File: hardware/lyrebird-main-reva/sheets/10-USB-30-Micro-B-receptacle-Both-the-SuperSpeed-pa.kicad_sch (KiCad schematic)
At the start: 4 parts, among them J1 Connfly DS1104-01

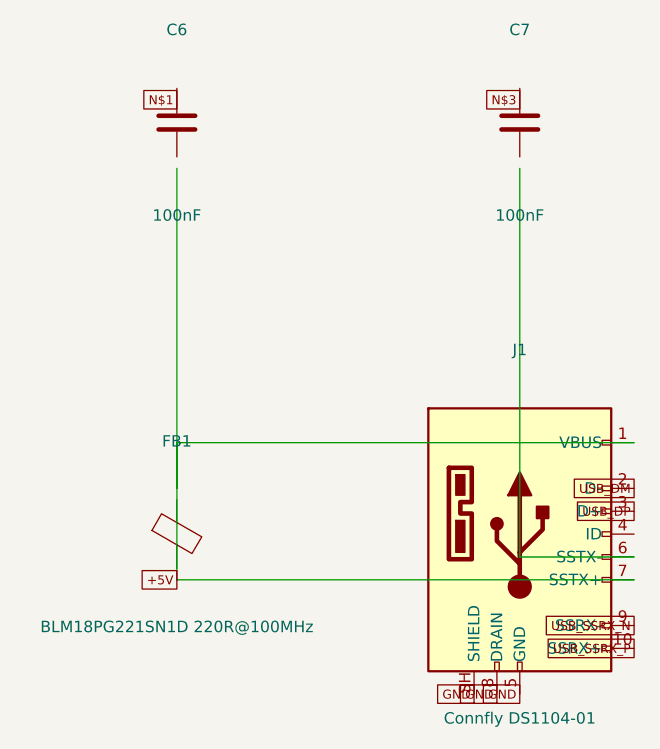
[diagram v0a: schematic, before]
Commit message: Regenerate the schematics, which were eleven days behind the netlists
The sheets and both PDFs dated 13 September against netlists from
today. They showed a board with USB bus power, a charge pump on the
analog module, no JTAG series protection, no oscillator pull-downs and
none of the footprint corrections -- a board that has not existed for
some time. Anyone opening them to review the design would have been
reviewing the wrong one, which is worse than having no schematic.

Regenerated from the current netlists: the main board goes from 8
sheets to 11, picking up the wall-wart input and the inverter, and the
module from 6 to 9 while losing the charge pump entirely. Both PDFs
rebuilt through kicad-cli, one page per sheet.

Nothing regenerated them because nothing was watching. The netlist
generators are run constantly and the views derived from them are not,
so they drift silently and there is no check that notices.

Co-Authored-By: Claude Opus 5 <noreply@anthropic.com>
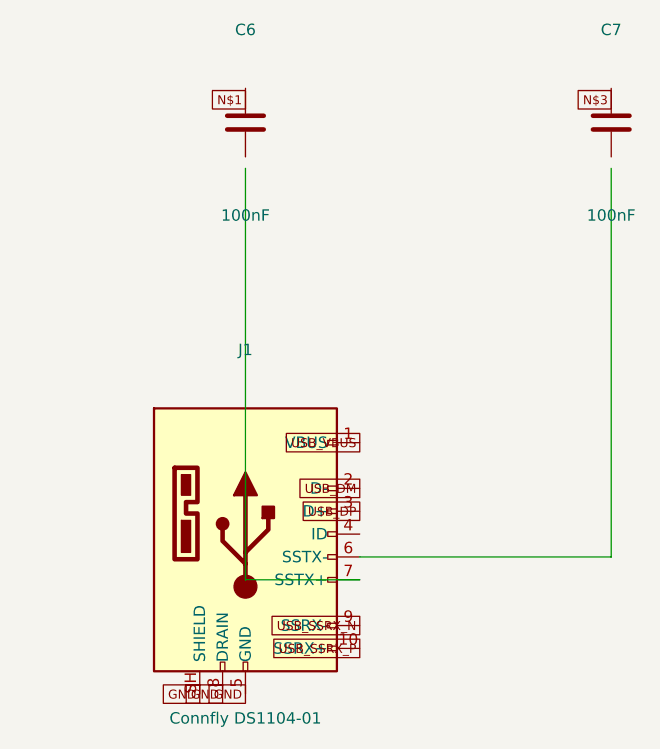
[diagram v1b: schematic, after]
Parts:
- removed J1: Connfly DS1104-01, symbol Connector:USB3_B_Micro
- J1: renamed from FB1; value BLM18PG221SN1D 220R@100MHz -> Connfly DS1104-01; symbol Device:FerriteBead -> Connector:USB3_B_Micro
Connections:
- net GND: now also J1.5 (GND), J1.8 (DRAIN), J1.SH (SHIELD)
- net USB_DM: now also J1.2 (D-)
- net USB_DP: now also J1.3 (D+)
- net USB_SSRX_N: now also J1.9 (SSRX-)
- net USB_SSRX_P: now also J1.10 (SSRX+)
- net USB_VBUS: now reaches J1.1 (VBUS)
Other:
- moved on the sheet: C6, C7
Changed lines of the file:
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@@
 	(paper "User" 132 128)
 	(title_block (title "USB 3.0 Micro-B receptacle. Both the SuperSpeed pairs and the"))
-	(symbol (lib_id "Device:C") (at 35.56 35.56 0) (unit 1)
+	(symbol (lib_id "Device:C") (at 43.18 35.56 0) (unit 1)
 		(exclude_from_sim no) (in_bom yes) (on_board yes) (dnp no)
-		(property "Reference" "C6" (at 35.56 25.250000000000004 0)
+		(property "Reference" "C6" (at 43.18 25.250000000000004 0)
 			(effects (font (size 1.27 1.27))))
-		(property "Value" "100nF" (at 35.56 45.870000000000005 0)
+		(property "Value" "100nF" (at 43.18 45.870000000000005 0)
 			(effects (font (size 1.27 1.27))))
 		(instances (project "" (path "/" (reference "C6") (unit 1))))
 	)
-	(symbol (lib_id "Device:C") (at 73.66 35.56 0) (unit 1)
+	(symbol (lib_id "Device:C") (at 83.82000000000001 35.56 0) (unit 1)
 		(exclude_from_sim no) (in_bom yes) (on_board yes) (dnp no)
-		(property "Reference" "C7" (at 73.66 25.250000000000004 0)
+		(property "Reference" "C7" (at 83.82000000000001 25.250000000000004 0)
 			(effects (font (size 1.27 1.27))))
-		(property "Value" "100nF" (at 73.66 45.870000000000005 0)
+		(property "Value" "100nF" (at 83.82000000000001 45.870000000000005 0)
 			(effects (font (size 1.27 1.27))))
 		(instances (project "" (path "/" (reference "C7") (unit 1))))
 	)
-	(symbol (lib_id "Device:FerriteBead") (at 35.56 81.28 0) (unit 1)
+	(symbol (lib_id "Connector:USB3_B_Micro") (at 43.18 81.28 0) (unit 1)
 		(exclude_from_sim no) (in_bom yes) (on_board yes) (dnp no)
-		(property "Reference" "FB1" (at 35.56 70.97 0)
+		(property "Reference" "J1" (at 43.18 60.81 0)
 			(effects (font (size 1.27 1.27))))
-		(property "Value" "BLM18PG221SN1D 220R@100MHz" (at 35.56 91.59 0)
-			(effects (font (size 1.27 1.27))))
-		(instances (project "" (path "/" (reference "FB1") (unit 1))))
-	)
-	(symbol (lib_id "Connector:USB3_B_Micro") (at 73.66 81.28 0) (unit 1)
-		(exclude_from_sim no) (in_bom yes) (on_board yes) (dnp no)
-		(property "Reference" "J1" (at 73.66 60.81 0)
-			(effects (font (size 1.27 1.27))))
-		(property "Value" "Connfly DS1104-01" (at 73.66 101.75 0)
+		(property "Value" "Connfly DS1104-01" (at 43.18 101.75 0)
 			(effects (font (size 1.27 1.27))))
 		(instances (project "" (path "/" (reference "J1") (unit 1))))
 	)
-	(wire (pts (xy 35.56 40.64) (xy 35.56 86.36))
+	(wire (pts (xy 43.18 40.64) (xy 43.18 86.36))
 		(stroke (width 0) (type default)))
-	(wire (pts (xy 35.56 86.36) (xy 86.36 86.36))
+	(wire (pts (xy 43.18 86.36) (xy 55.88 86.36))
 		(stroke (width 0) (type default)))
-	(wire (pts (xy 73.66 40.64) (xy 73.66 83.82000000000001))
+	(wire (pts (xy 83.82000000000001 40.64) (xy 83.82000000000001 83.82000000000001))
 		(stroke (width 0) (type default)))
-	(wire (pts (xy 73.66 83.82000000000001) (xy 86.36 83.82000000000001))
+	(wire (pts (xy 83.82000000000001 83.82000000000001) (xy 55.88 83.82000000000001))
 		(stroke (width 0) (type default)))
-	(wire (pts (xy 35.56 76.2) (xy 35.56 71.12))
-		(stroke (width 0) (type default)))
-	(wire (pts (xy 35.56 71.12) (xy 86.36 71.12))
-		(stroke (width 0) (type default)))
-	(global_label "+5V" (shape passive) (at 35.56 86.36 0)
+	(global_label "GND" (shape passive) (at 43.18 99.06 0)
 		(effects (font (size 1.0 1.0)) (justify right))
 )
-	(global_label "GND" (shape passive) (at 73.66 99.06 0)
+	(global_label "GND" (shape passive) (at 40.64 99.06 0)
 		(effects (font (size 1.0 1.0)) (justify right))
 )
-	(global_label "GND" (shape passive) (at 71.12 99.06 0)
+	(global_label "GND" (shape passive) (at 38.1 99.06 0)
 		(effects (font (size 1.0 1.0)) (justify right))
 )
-	(global_label "GND" (shape passive) (at 68.58 99.06 0)
+	(global_label "N$1" (shape passive) (at 43.18 33.02 0)
 		(effects (font (size 1.0 1.0)) (justify right))
 )
-	(global_label "N$1" (shape passive) (at 35.56 33.02 0)
+	(global_label "N$3" (shape passive) (at 83.82000000000001 33.02 0)
 		(effects (font (size 1.0 1.0)) (justify right))
 )
-	(global_label "N$3" (shape passive) (at 73.66 33.02 0)
+	(global_label "USB_DM" (shape passive) (at 55.88 76.2 0)
 		(effects (font (size 1.0 1.0)) (justify right))
 )
-	(global_label "USB_DM" (shape passive) (at 86.36 76.2 0)
+	(global_label "USB_DP" (shape passive) (at 55.88 78.74 0)
 		(effects (font (size 1.0 1.0)) (justify right))
 )
-	(global_label "USB_DP" (shape passive) (at 86.36 78.74 0)
+	(global_label "USB_SSRX_N" (shape passive) (at 55.88 91.44 0)
 		(effects (font (size 1.0 1.0)) (justify right))
 )
-	(global_label "USB_SSRX_N" (shape passive) (at 86.36 91.44 0)
+	(global_label "USB_SSRX_P" (shape passive) (at 55.88 93.98 0)
 		(effects (font (size 1.0 1.0)) (justify right))
 )
-	(global_label "USB_SSRX_P" (shape passive) (at 86.36 93.98 0)
+	(global_label "USB_VBUS" (shape passive) (at 55.88 71.12 0)
 		(effects (font (size 1.0 1.0)) (justify right))
 )
